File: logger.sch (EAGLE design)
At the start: 77 parts, among them IC1 LTC4412, J1 POWER_JACKPTH, Q1 FDN360P, Q2 FDN360P, Q3 2N7002PW, Q4 2N7002PW, U1 DS3231MZ/V+T, U2 FT231X-Q

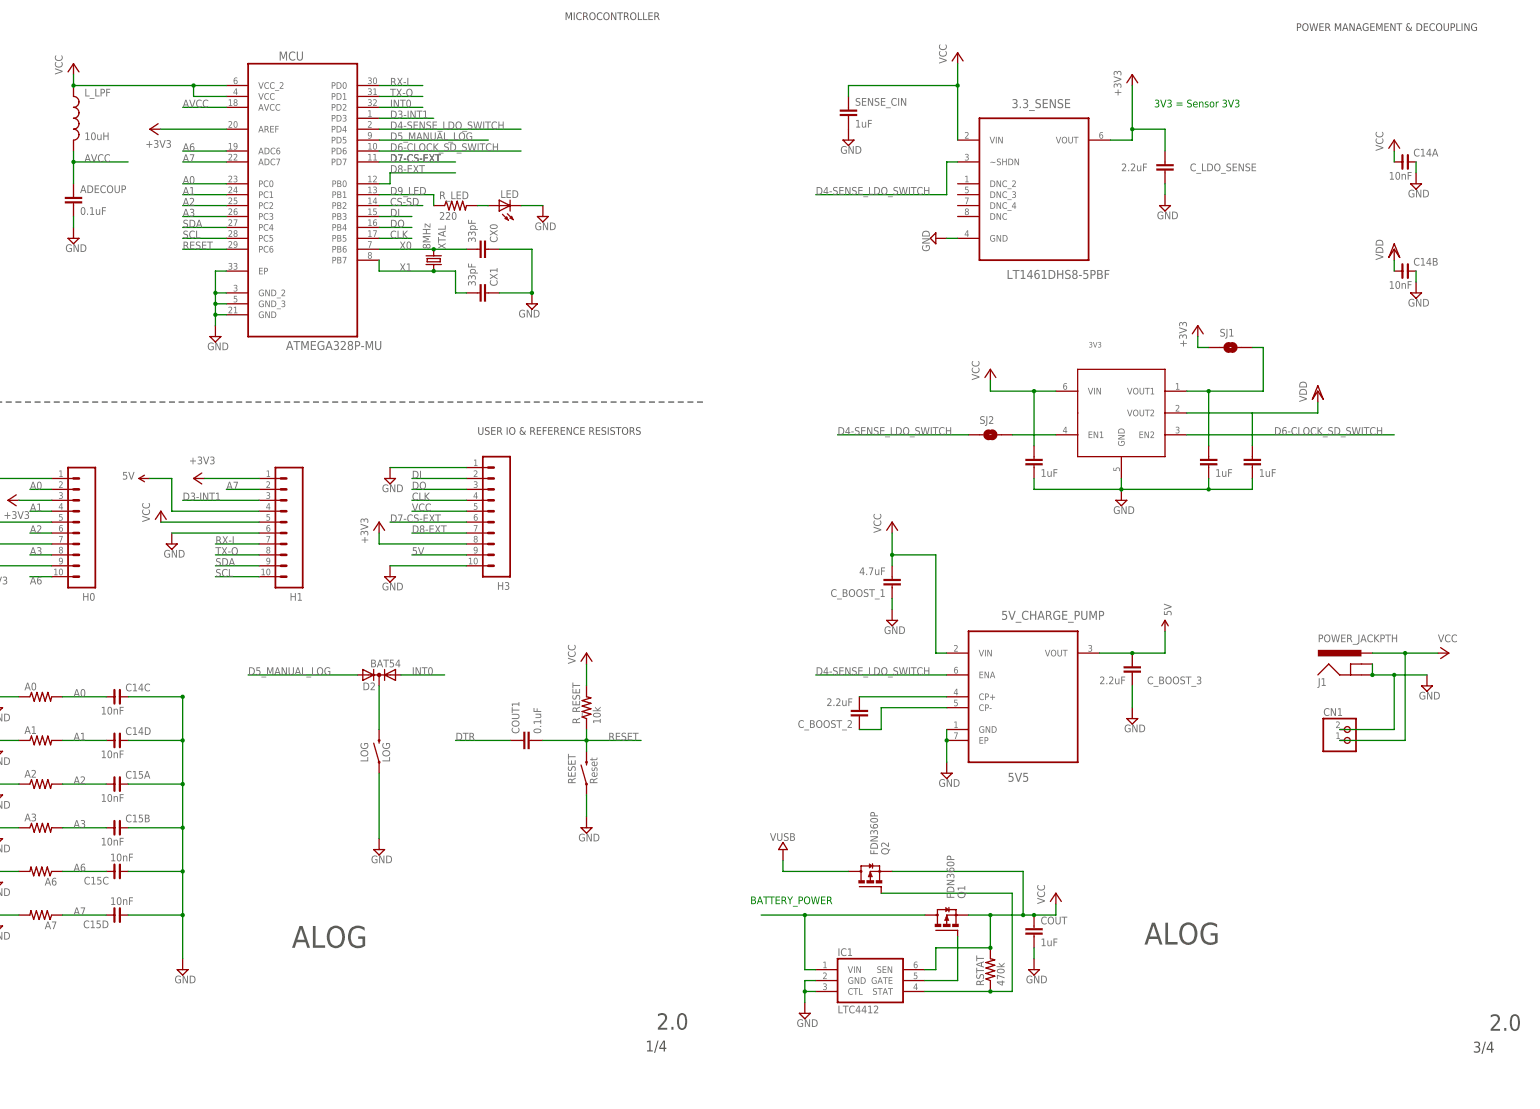
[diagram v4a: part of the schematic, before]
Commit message: Routed new layout, no precision 3V3
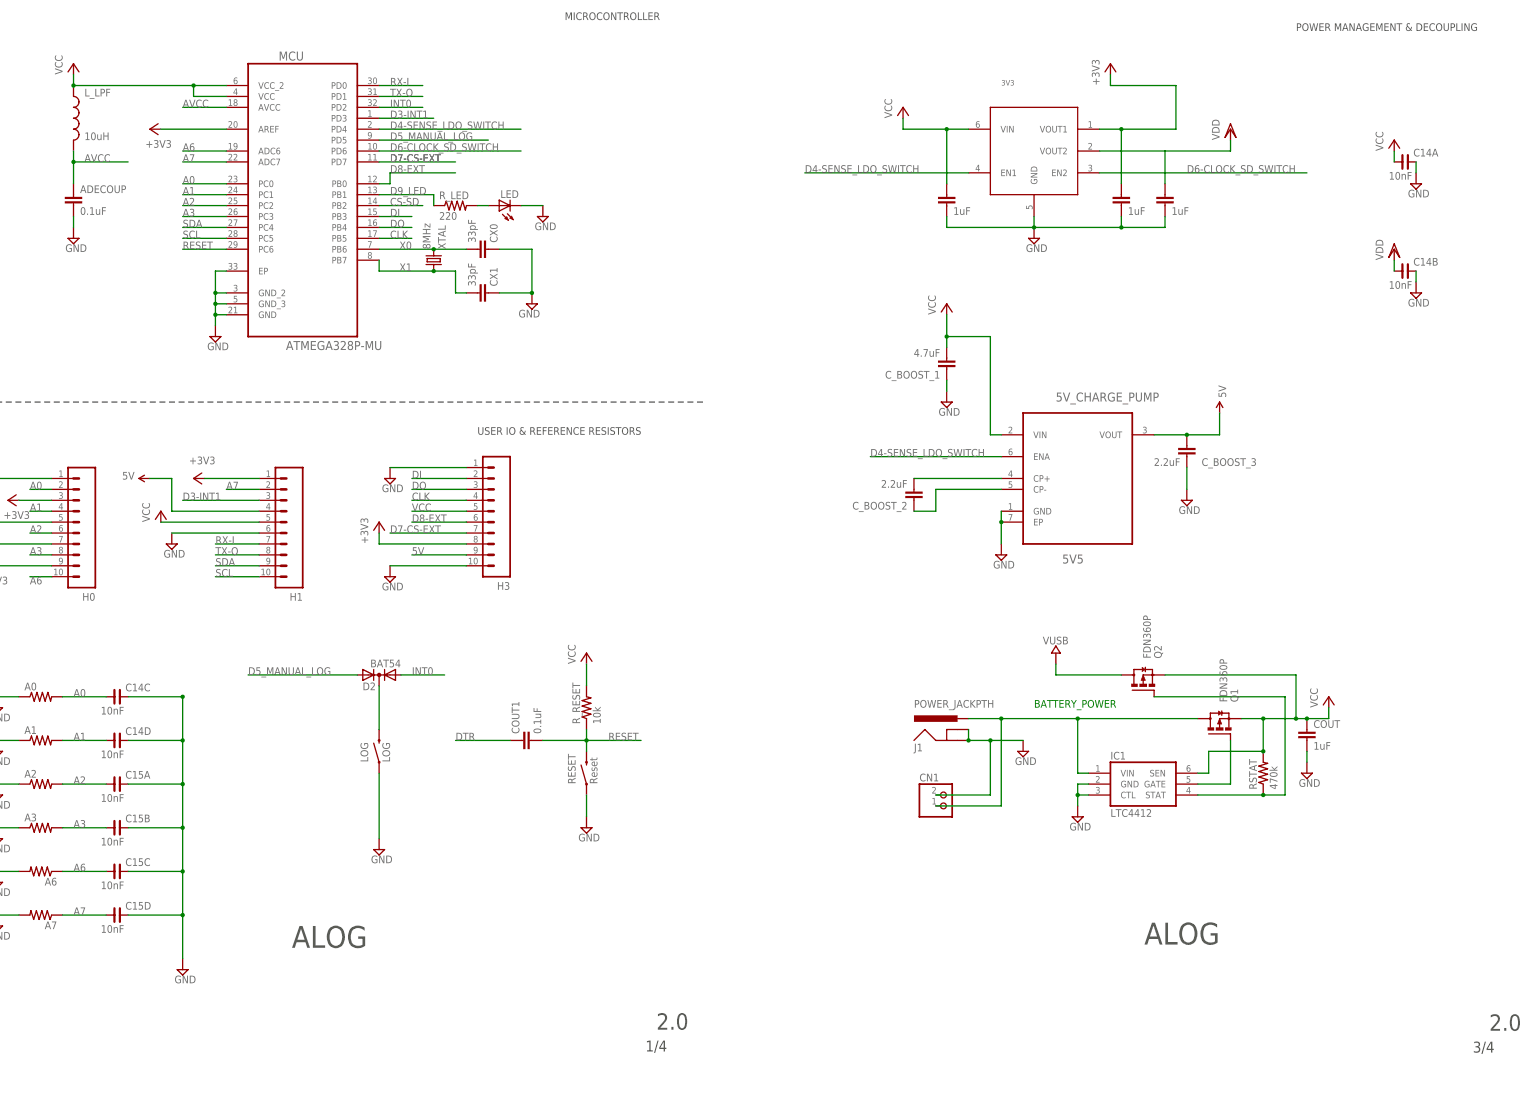
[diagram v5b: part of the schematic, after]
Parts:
- removed 3.3_SENSE: LT1461DHS8-5PBF, LTC_By_element14_Batch_1:LT1461DHS8-5PBF
- removed C_LDO_SENSE: 2.2uF, resistor:C-EUC0603
- removed SENSE_CIN: 1uF, rcl:C-EUC0603
- removed SJ1, SJ2: SOLDERJUMPERNO, SparkFun-Retired:SOLDERJUMPERNO
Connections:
- removed net N$19: 3V3.EN1, SJ2.2
- removed net N$20: 3V3.VOUT1, CLOCK_CIN2.1, SJ1.2
- new net VBAT: CN1.2, IC1.VIN, J1.PWR, Q1.D
- net +3V3: now also 3V3.VOUT1, CLOCK_CIN2.1; no longer 3.3_SENSE.VOUT, C_LDO_SENSE.2, SJ1.1
- net A6: now also C15C.1; no longer C15C.2
- net A7: now also C15D.1; no longer C15D.2
- net D4-SENSE_LDO_SWITCH: now also 3V3.EN1; no longer 3.3_SENSE.~SHDN, SJ2.1
- net D7-CS-EXT: now also H3.7; no longer H3.6
- net D8-EXT: now also H3.6; no longer H3.7
- net GND: now also C15C.2, C15D.2; no longer 3.3_SENSE.GND, C15C.1, C15D.1, C_LDO_SENSE.1, SENSE_CIN.2
- net VCC: no longer 3.3_SENSE.VIN, CN1.2, IC1.VIN, J1.PWR, Q1.D, SENSE_CIN.1
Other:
- note removed: "3V3 = Sensor 3V3"
- moved on the sheet: 3V3, 5V_CHARGE_PUMP, C15C, C15D, CN1, COUT, C_BOOST_1, C_BOOST_2, C_BOOST_3, IC1, J1, Q1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

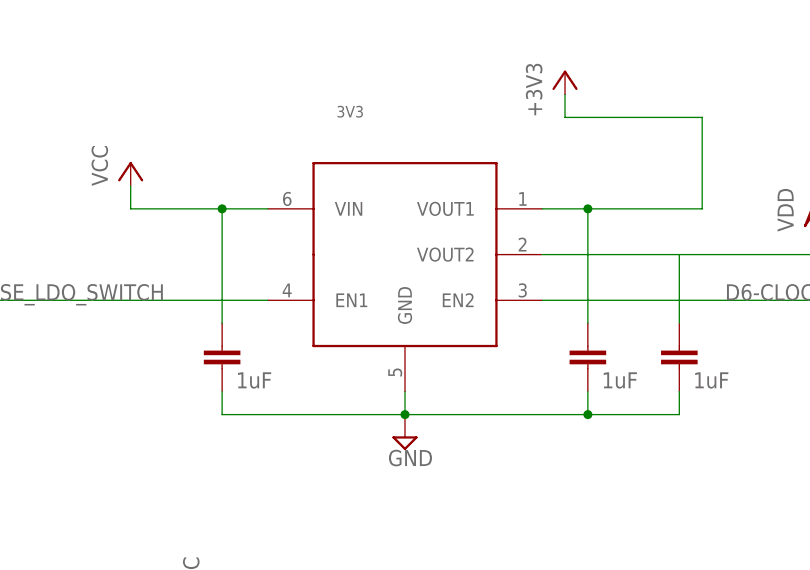
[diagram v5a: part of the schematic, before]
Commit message: increased pad sizes for 3V3
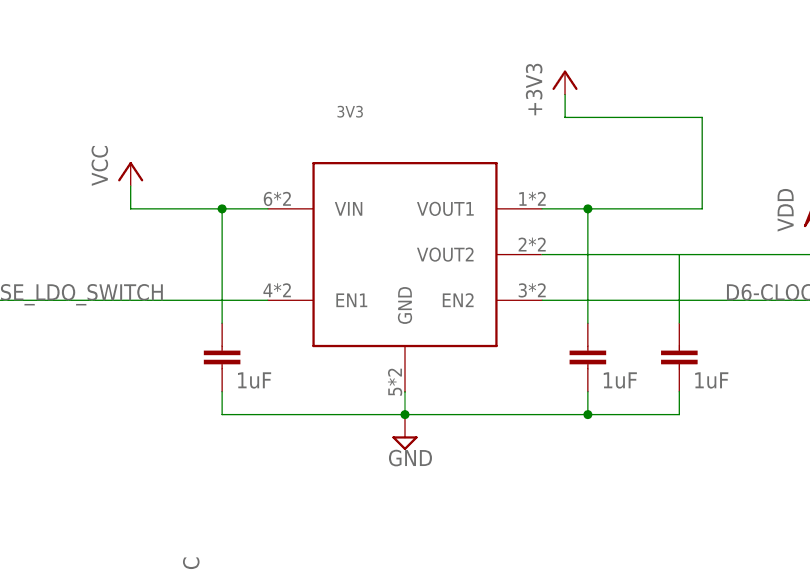
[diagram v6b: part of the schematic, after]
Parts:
- 3V3: device csandell:MIC5380 -> logger:MIC5380
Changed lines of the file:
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@@
 <part name="FRAME5" library="frames" deviceset="LETTER_P" device=""/>
 <part name="CN1" library="adafruit" deviceset="JST_2PIN" device="-THM"/>
-<part name="3V3" library="csandell" deviceset="MIC5380" device=""/>
 <part name="CLOCK_CIN1" library="rcl" deviceset="C-EU" device="C0603" value="1uF"/>
 <part name="CLOCK_CIN2" library="rcl" deviceset="C-EU" device="C0603" value="1uF"/>
@@
 <part name="SD_3V5" library="supply1" deviceset="VDD" device=""/>
 <part name="SD_3V6" library="supply1" deviceset="VDD" device=""/>
+<part name="3V3" library="logger" deviceset="MIC5380" device=""/>
 </parts>
 <sheets>
@@
 </instance>
 <instance part="CN1" gate="G$1" x="571.5" y="25.4"/>
-<instance part="3V3" gate="G$1" x="591.82" y="177.8"/>
 <instance part="CLOCK_CIN1" gate="G$1" x="571.5" y="167.64" smashed="yes">
 <attribute name="VALUE" x="573.024" y="162.941" size="1.778" layer="96"/>
@@
 <instance part="SD_3V5" gate="G$1" x="444.5" y="-170.18"/>
 <instance part="SD_3V6" gate="G$1" x="342.9" y="-185.42"/>
+<instance part="3V3" gate="G$1" x="591.82" y="177.8"/>
 </instances>
 <busses>
@@
 </segment>
 <segment>
-<pinref part="3V3" gate="G$1" pin="VIN"/>
 <wire x1="576.58" y1="182.88" x2="571.5" y2="182.88" width="0.1524" layer="91"/>
 <wire x1="571.5" y1="182.88" x2="561.34" y2="182.88" width="0.1524" layer="91"/>
@@
 <pinref part="P+9" gate="VCC" pin="VCC"/>
 <wire x1="561.34" y1="182.88" x2="561.34" y2="185.42" width="0.1524" layer="91"/>
+<pinref part="3V3" gate="G$1" pin="VIN"/>
 </segment>
 </net>
@@
 <pinref part="+3V3" gate="G$1" pin="+3V3"/>
 <wire x1="609.6" y1="195.58" x2="609.6" y2="193.04" width="0.1524" layer="91"/>
-<pinref part="3V3" gate="G$1" pin="VOUT1"/>
 <wire x1="607.06" y1="182.88" x2="612.14" y2="182.88" width="0.1524" layer="91"/>
 <pinref part="CLOCK_CIN2" gate="G$1" pin="1"/>
@@
 <wire x1="624.84" y1="182.88" x2="624.84" y2="193.04" width="0.1524" layer="91"/>
 <wire x1="624.84" y1="193.04" x2="609.6" y2="193.04" width="0.1524" layer="91"/>
+<pinref part="3V3" gate="G$1" pin="VOUT1"/>
 </segment>
 <segment>
@@
 </segment>
 <segment>
-<pinref part="3V3" gate="G$1" pin="VOUT2"/>
 <wire x1="607.06" y1="177.8" x2="622.3" y2="177.8" width="0.1524" layer="91"/>
 <pinref part="CLOCK_CIN3" gate="G$1" pin="1"/>
@@
 <pinref part="SD_3V1" gate="G$1" pin="VDD"/>
 <wire x1="637.54" y1="177.8" x2="637.54" y2="180.34" width="0.1524" layer="91"/>
+<pinref part="3V3" gate="G$1" pin="VOUT2"/>
 </segment>
 <segment>
@@
 </segment>
 <segment>
-<pinref part="3V3" gate="G$1" pin="GND"/>
 <wire x1="591.82" y1="162.56" x2="591.82" y2="160.02" width="0.1524" layer="91"/>
 <wire x1="591.82" y1="160.02" x2="612.14" y2="160.02" width="0.1524" layer="91"/>
@@
 <wire x1="571.5" y1="162.56" x2="571.5" y2="160.02" width="0.1524" layer="91"/>
 <junction x="612.14" y="160.02"/>
+<pinref part="3V3" gate="G$1" pin="GND"/>
 </segment>
 <segment>
@@
 </segment>
 <segment>
-<pinref part="3V3" gate="G$1" pin="EN2"/>
 <wire x1="607.06" y1="172.72" x2="655.32" y2="172.72" width="0.1524" layer="91"/>
 <label x="627.38" y="172.72" size="1.778" layer="95"/>
-</segment>
-</net>
+<pinref part="3V3" gate="G$1" pin="EN2"/>
+</segment>
+</net>

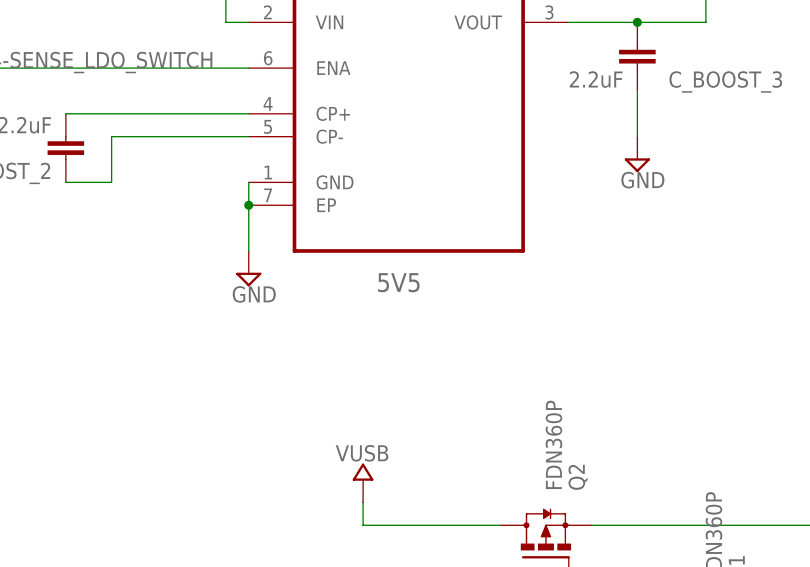
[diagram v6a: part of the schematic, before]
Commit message: 5V5 --> 5V
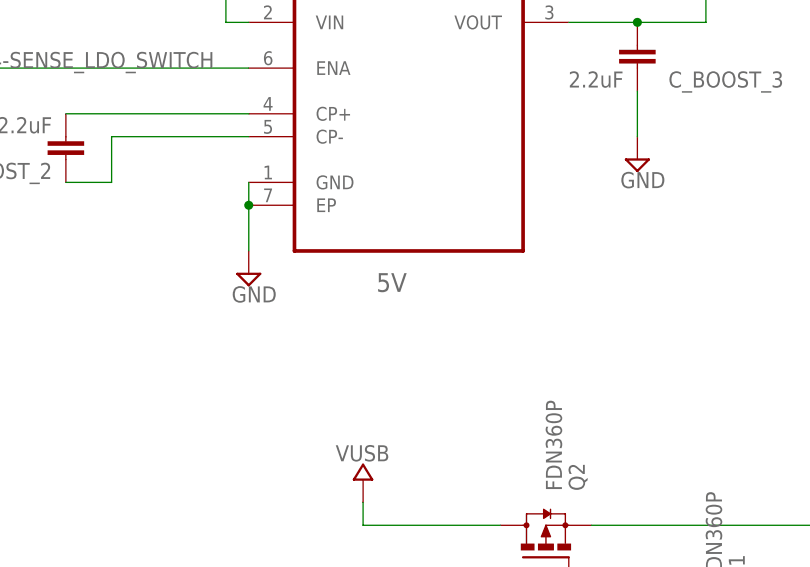
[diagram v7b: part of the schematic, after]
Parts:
- 5V_CHARGE_PUMP: value 5V5 -> 5V
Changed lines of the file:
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@@
 <part name="SUPPLY41" library="supply2" deviceset="GND" device=""/>
 <part name="5V1" library="SparkFun-Aesthetics" deviceset="5V" device=""/>
-<part name="5V_CHARGE_PUMP" library="ti_by_element14" deviceset="TPS60150DRVR" device="" value="5V5"/>
+<part name="5V_CHARGE_PUMP" library="ti_by_element14" deviceset="TPS60150DRVR" device="" value="5V"/>
 <part name="C_BOOST_1" library="resistor" deviceset="C-EU" device="C0603" value="4.7uF"/>
 <part name="C_BOOST_3" library="resistor" deviceset="C-EU" device="C0603" value="2.2uF"/>

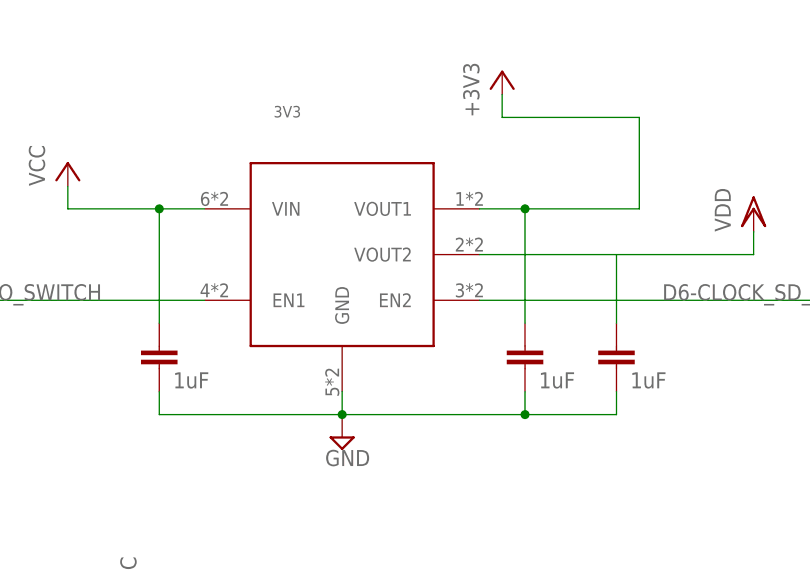
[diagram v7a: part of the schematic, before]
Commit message: Create custom pads for 3V3 output voltage chip
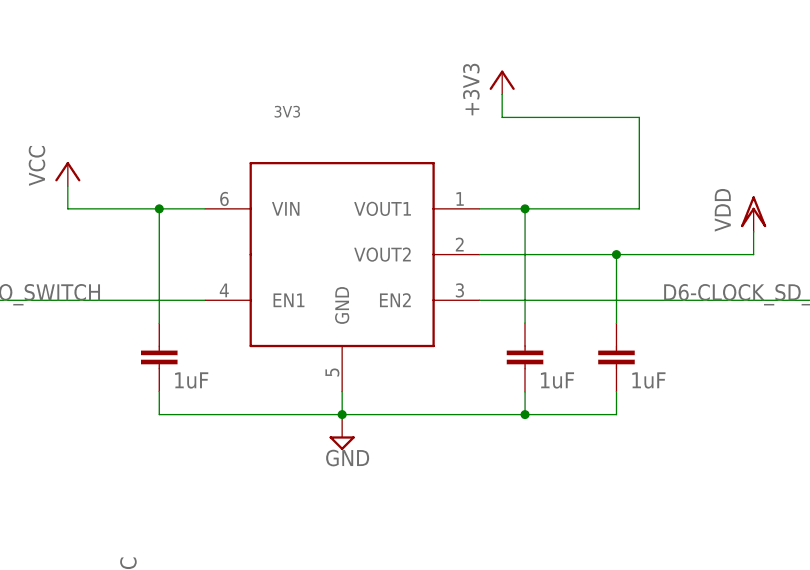
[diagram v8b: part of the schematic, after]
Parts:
- 3V3: device logger:MIC5380 -> csandell:MIC5380
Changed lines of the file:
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@@
 <part name="SD_3V5" library="supply1" deviceset="VDD" device=""/>
 <part name="SD_3V6" library="supply1" deviceset="VDD" device=""/>
-<part name="3V3" library="logger" deviceset="MIC5380" device=""/>
+<part name="3V3" library="csandell" deviceset="MIC5380" device=""/>
 </parts>
 <sheets>
@@
 <wire x1="637.54" y1="177.8" x2="637.54" y2="180.34" width="0.1524" layer="91"/>
 <pinref part="3V3" gate="G$1" pin="VOUT2"/>
+<junction x="622.3" y="177.8"/>
 </segment>
 <segment>
@@
 </sheet>
 </sheets>
+<errors>
+</errors>
 </schematic>
 </drawing>
